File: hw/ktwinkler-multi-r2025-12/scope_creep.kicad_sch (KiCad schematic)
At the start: 1 part, among them J12 Connector_HAN_P1

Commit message: this is just getting silly
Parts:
- added JP4: KJumper_2, TestPoint:TestPoint_2Pads_Pitch2.54mm_Drill0.8mm, symbol karl-parts:KJumper_2
- added Q1: 2N7002, Package_TO_SOT_SMD:SOT-23, symbol karl-atomic-basic:BSS138
- added R13, R17: 0R, Resistor_SMD:R_0402_1005Metric, symbol karl-atomic-basic:KR0402_0R
- added R18: 10k, Resistor_SMD:R_0402_1005Metric, symbol karl-atomic-basic:KR0402_10k
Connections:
- net +5V: now also JP4.1 (A), R13.2
- net GND: now also Q1.2 (S)
- net P1_OUT: now also Q1.3 (D), R18.2; no longer J12.5 (DATA)
- net P1_REQ: now also R13.1
- new net: Q1.1 (G), R17.2
- new net +3V3: R18.1
- new net +BATT: JP4.2 (B)
- new net P1_OUT_RAW: J12.5 (DATA), R17.1
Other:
- note added: "Lots of other people's hardware just hard turn this on"

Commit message: "schematic complete" (lol)
but yeah, i think this is most of it?  time to maybe route shit?
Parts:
- removed Q1: 2N7002, Package_TO_SOT_SMD:SOT-23, symbol karl-atomic-basic:BSS138
- added Q1, Q4: HL3400A, Package_TO_SOT_SMD:SOT-23, symbol karl-atomic-basic:Mosfet_HL3400A
- added Q3: HL2301A, Package_TO_SOT_SMD:SOT-23, symbol karl-atomic-basic:Mosfet_HL2301A
- added R21: 0R, Resistor_SMD:R_0402_1005Metric, symbol karl-atomic-basic:KR0402_0R
- added R22: 10k, Resistor_SMD:R_0402_1005Metric, symbol karl-atomic-basic:KR0402_10k
- R13: now not fitted
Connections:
- net +5V: now also Q3.2 (S), R22.1
- net GND: now also Q1.2 (S), Q4.2 (S)
- net P1_OUT: now also Q4.3 (D)
- net P1_REQ: now also R21.1
- net at R17.2: now also Q4.1 (G)
- new net: Q1.3 (D), Q3.1 (G), R22.2
- new net: Q3.3 (D), R21.2
- new net P1_Do_Request: Q1.1 (G)

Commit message: hw: save before kicad 10 upgrade
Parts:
- J12: now left out of the parts list
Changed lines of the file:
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@@
 		(unit 1)
 		(exclude_from_sim no)
-		(in_bom yes)
+		(in_bom no)
 		(on_board yes)
 		(dnp no)

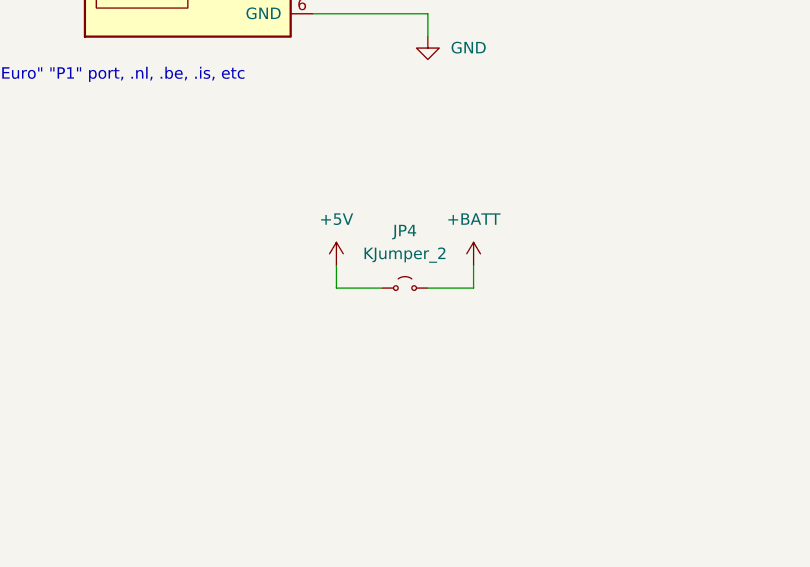
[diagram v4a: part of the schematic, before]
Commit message: hw: update to kicad 10 and order
We added a late qwiic connector to the ch584 side, why not, try that out
too.  We also fixed our smtso footprint, we hope...

Fuck poking the rf more, we're yolo-poling...
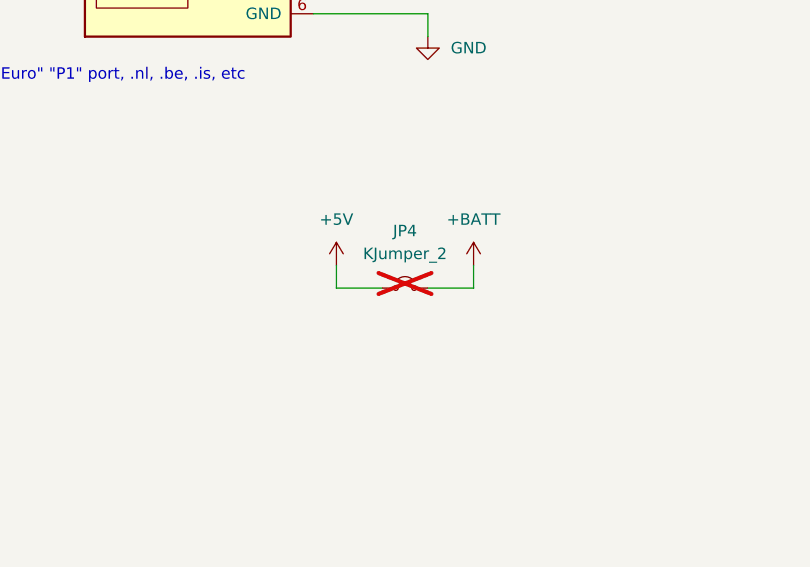
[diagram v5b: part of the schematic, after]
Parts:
- JP4: now not fitted
